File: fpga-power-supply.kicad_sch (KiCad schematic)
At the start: 30 parts, among them U14 XC7A100T-FGG484

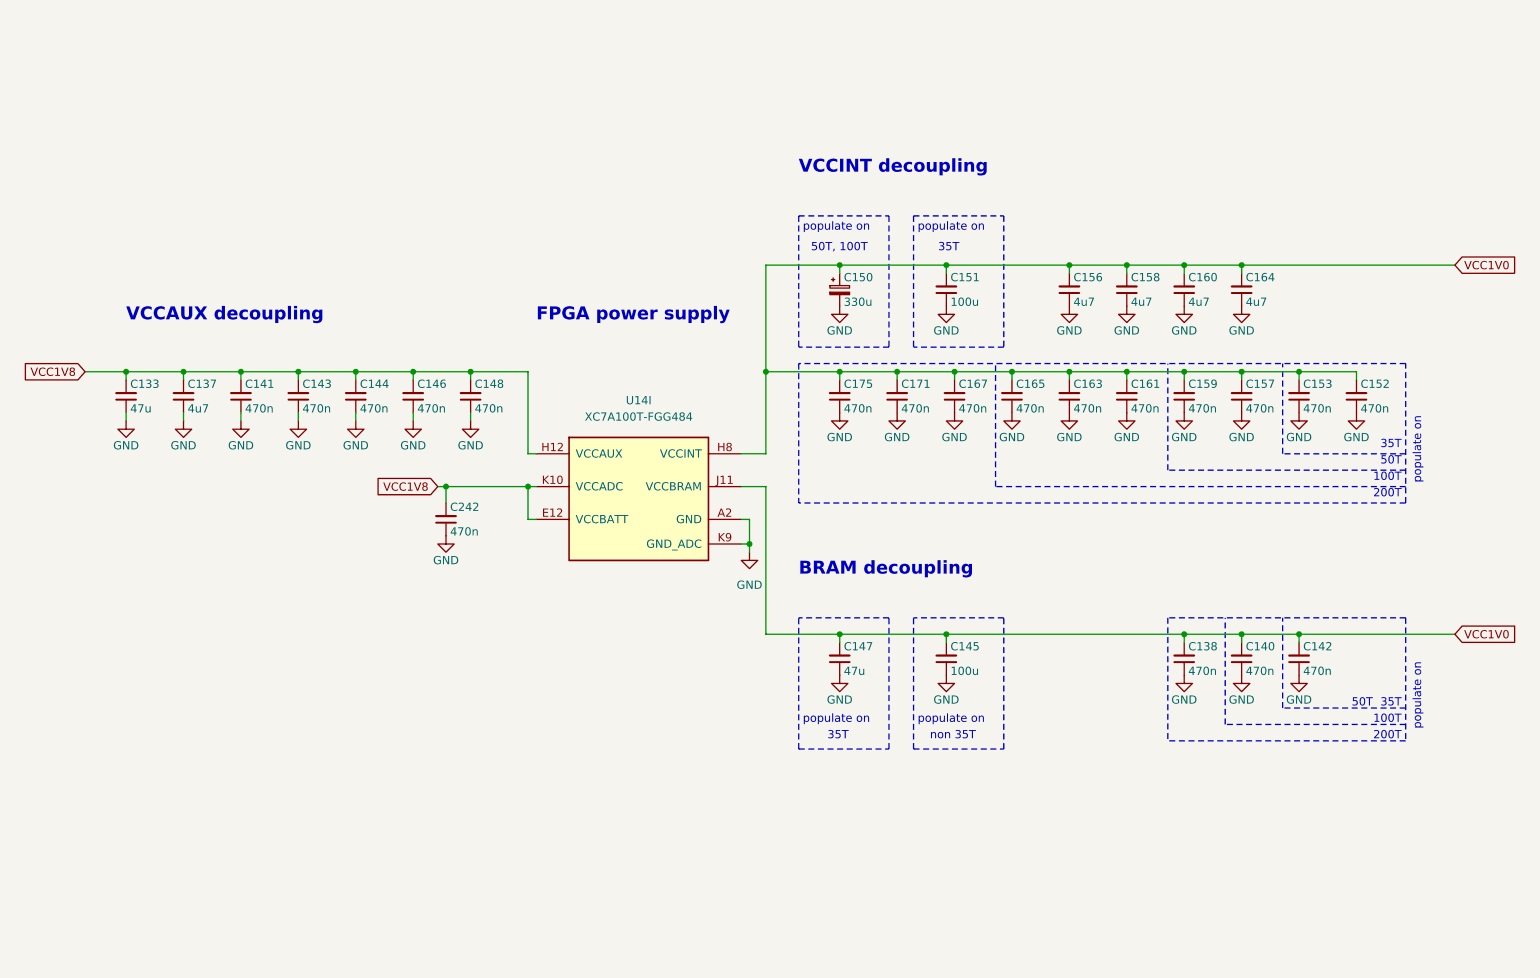
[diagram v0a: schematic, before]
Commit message: [#68236] Update symbols and footprints, clean ERC and DRC
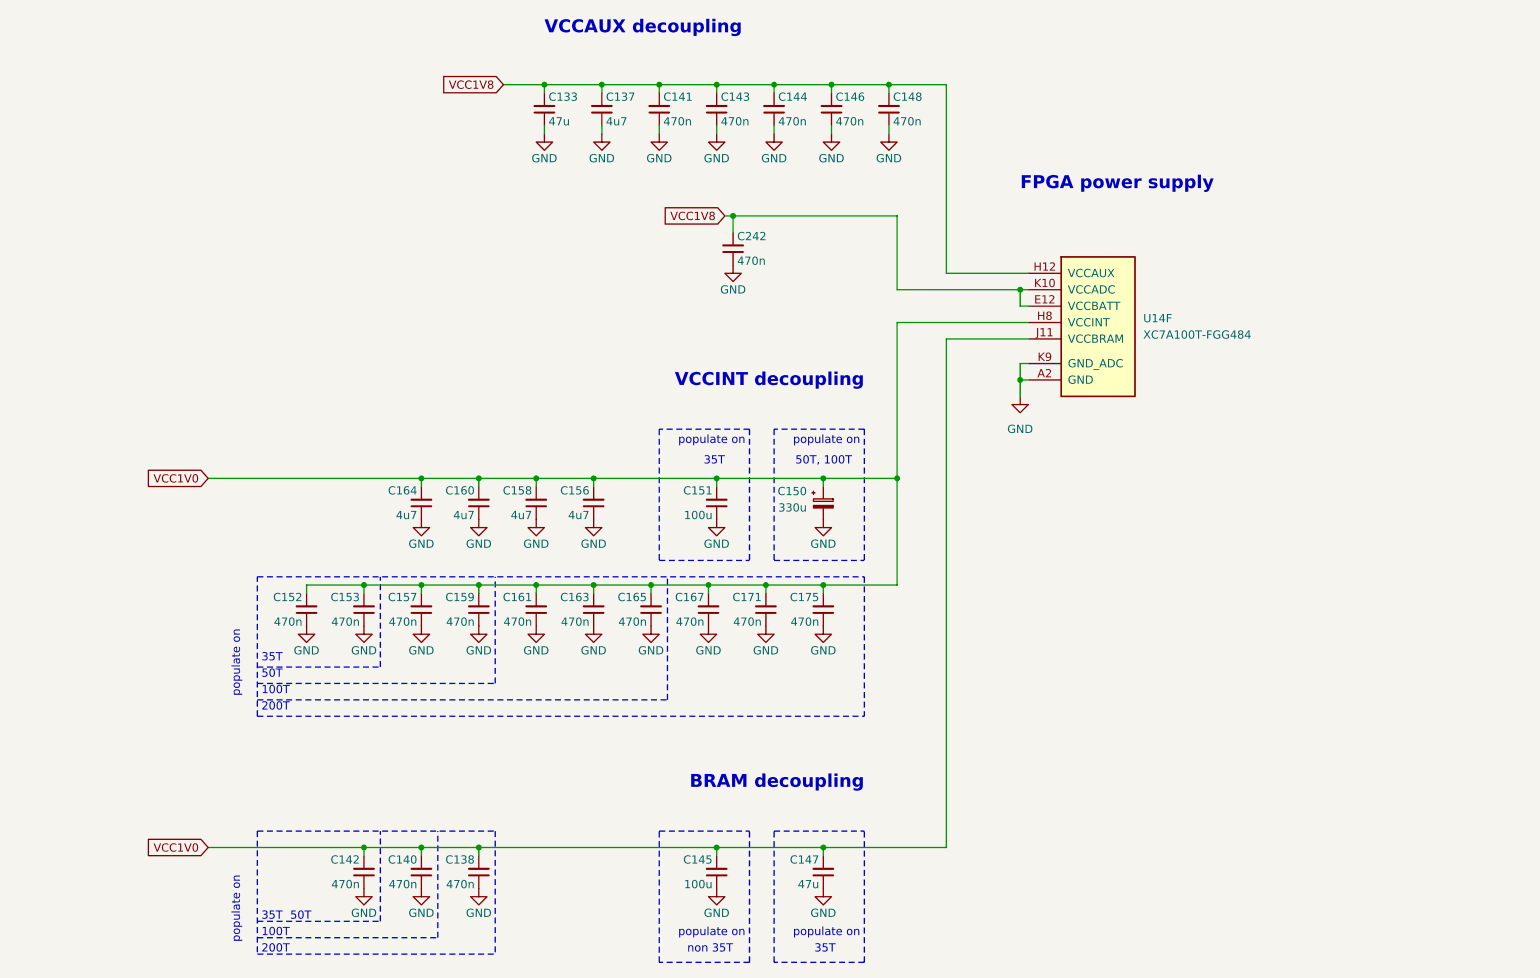
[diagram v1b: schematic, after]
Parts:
- removed U14: XC7A100T-FGG484, antmicro-footprints:BGA-484_23x23mm_Layout22x22_P1mm_FGG484, symbol antmicroFPGAChips:XC7A100T-FGG484
- added U14: XC7A100T-FGG484, antmicro-footprints:BGA-484_23x23mm_Layout22x22_P1mm_FGG484, symbol antmicroFPGAChips:XC7A100T-FGG484
- C133, C138, C142, C145, C146, C147, C151, C152, C153, C157, C159, C161, C163, C165, C171, C175, C242: Public (none) -> False
- C150: Dielectric (none) -> template_dielectric
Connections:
- net GND: now also U14.A11 (GND), U14.A12 (GND), U14.A2 (GND), U14.A22 (GND), U14.A3 (GND), U14.A5 (GND), U14.A7 (GND), U14.A9 (GND), U14.AA12 (GND), U14.AA2 (GND), U14.AA22 (GND), U14.AB19 (GND), U14.AB9 (GND), U14.B12 (GND), U14.B19 (GND), U14.B3 (GND), U14.C10 (GND), U14.C12 (GND), U14.C16 (GND), U14.C3 (GND), U14.C6 (GND), U14.D12 (GND), U14.D13 (GND), U14.D3 (GND), U14.D4 (GND), U14.D8 (GND), U14.E11 (GND), U14.E20 (GND), U14.E4 (GND), U14.E5 (GND), U14.E7 (GND), U14.E9 (GND), U14.F11 (GND), U14.F17 (GND), U14.F5 (GND), U14.G10 (GND), U14.G12 (GND), U14.G14 (GND), U14.G5 (GND), U14.G6 (GND), U14.G7 (GND), U14.G8 (GND), U14.G9 (GND), U14.H1 (GND), U14.H11 (GND), U14.H21 (GND), U14.H7 (GND), U14.H9 (GND), U14.J10 (GND), U14.J12 (GND), U14.J18 (GND), U14.J8 (GND), U14.K11 (GND), U14.K15 (GND), U14.K5 (GND), U14.K7 (GND), U14.K9 (GND_ADC), U14.L2 (GND), U14.L22 (GND), U14.L8 (GND), U14.M11 (GND), U14.M19 (GND), U14.M7 (GND), U14.N16 (GND), U14.N6 (GND), U14.N8 (GND), U14.P11 (GND), U14.P13 (GND), U14.P3 (GND), U14.P7 (GND), U14.P9 (GND), U14.R10 (GND), U14.R12 (GND), U14.R20 (GND), U14.R8 (GND), U14.T11 (GND), U14.T17 (GND), U14.T7 (GND), U14.T9 (GND), U14.U14 (GND), U14.U4 (GND), U14.V1 (GND), U14.V11 (GND), U14.V21 (GND), U14.W18 (GND), U14.W8 (GND), U14.Y15 (GND), U14.Y5 (GND)
- net VCC1V0: now also U14.H10 (VCCINT), U14.H8 (VCCINT), U14.J11 (VCCBRAM), U14.J7 (VCCINT), U14.J9 (VCCINT), U14.K8 (VCCINT), U14.L11 (VCCBRAM), U14.L7 (VCCINT), U14.M8 (VCCINT), U14.N11 (VCCBRAM), U14.N7 (VCCINT), U14.P10 (VCCINT), U14.P8 (VCCINT), U14.R7 (VCCINT), U14.R9 (VCCINT), U14.T10 (VCCINT), U14.T8 (VCCINT)
- net VCC1V8: now also U14.E12 (VCCBATT), U14.H12 (VCCAUX), U14.K10 (VCCADC), U14.K12 (VCCAUX), U14.M12 (VCCAUX), U14.P12 (VCCAUX), U14.R11 (VCCAUX)
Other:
- moved on the sheet: C133, C137, C141, C143, C144, C146, C148, C242

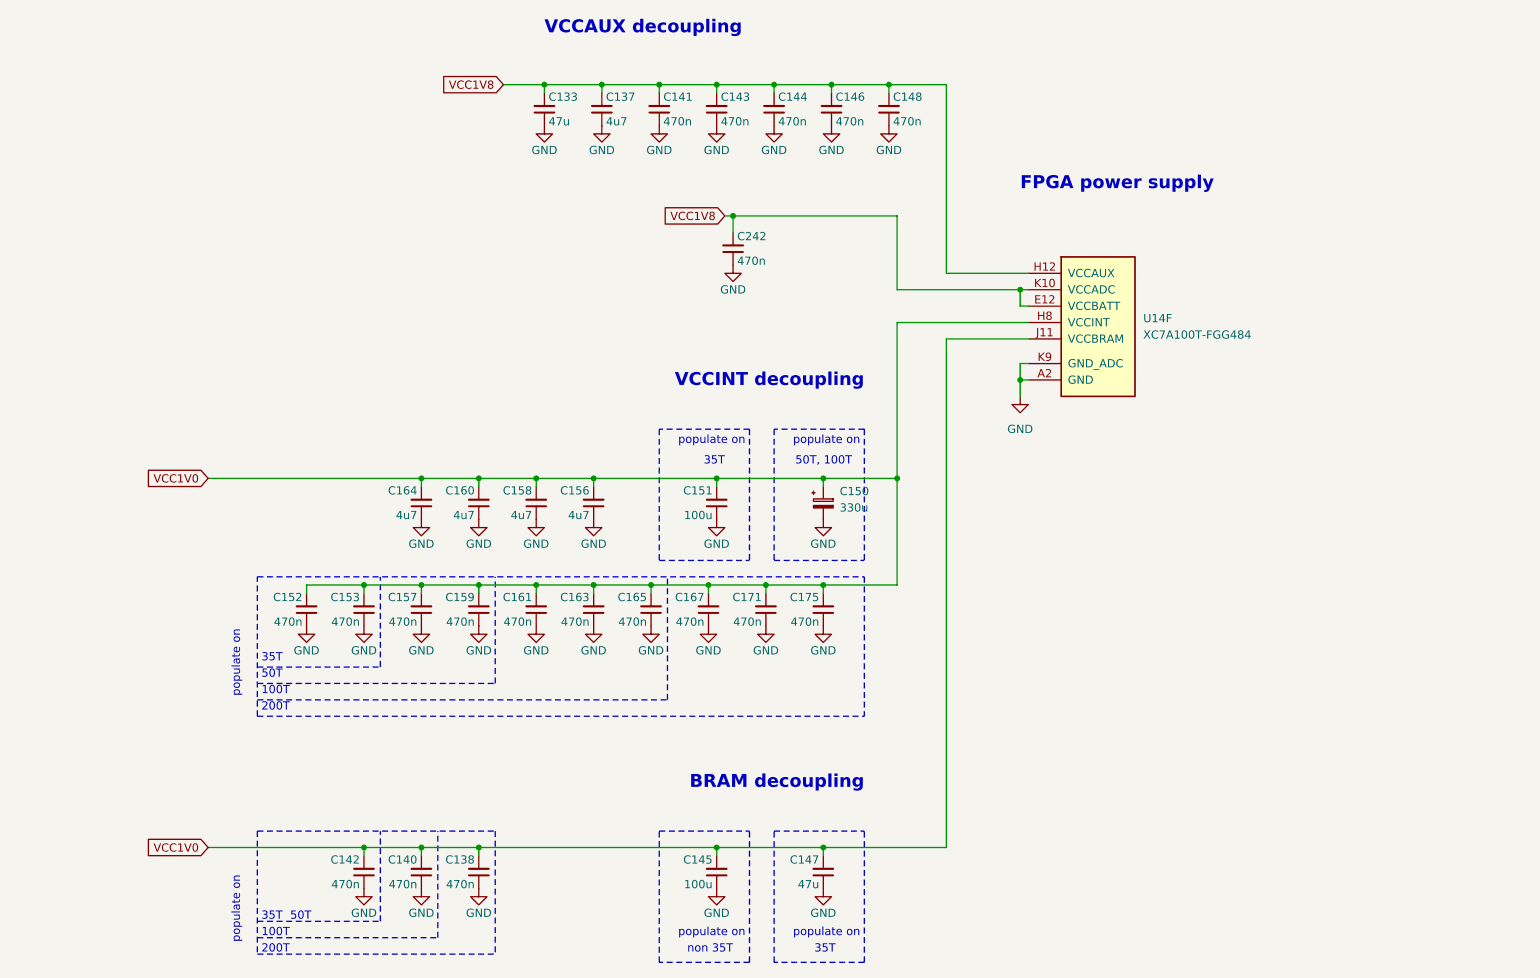
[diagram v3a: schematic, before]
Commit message: a lot of routing and almost all caps of the fpga are placed down
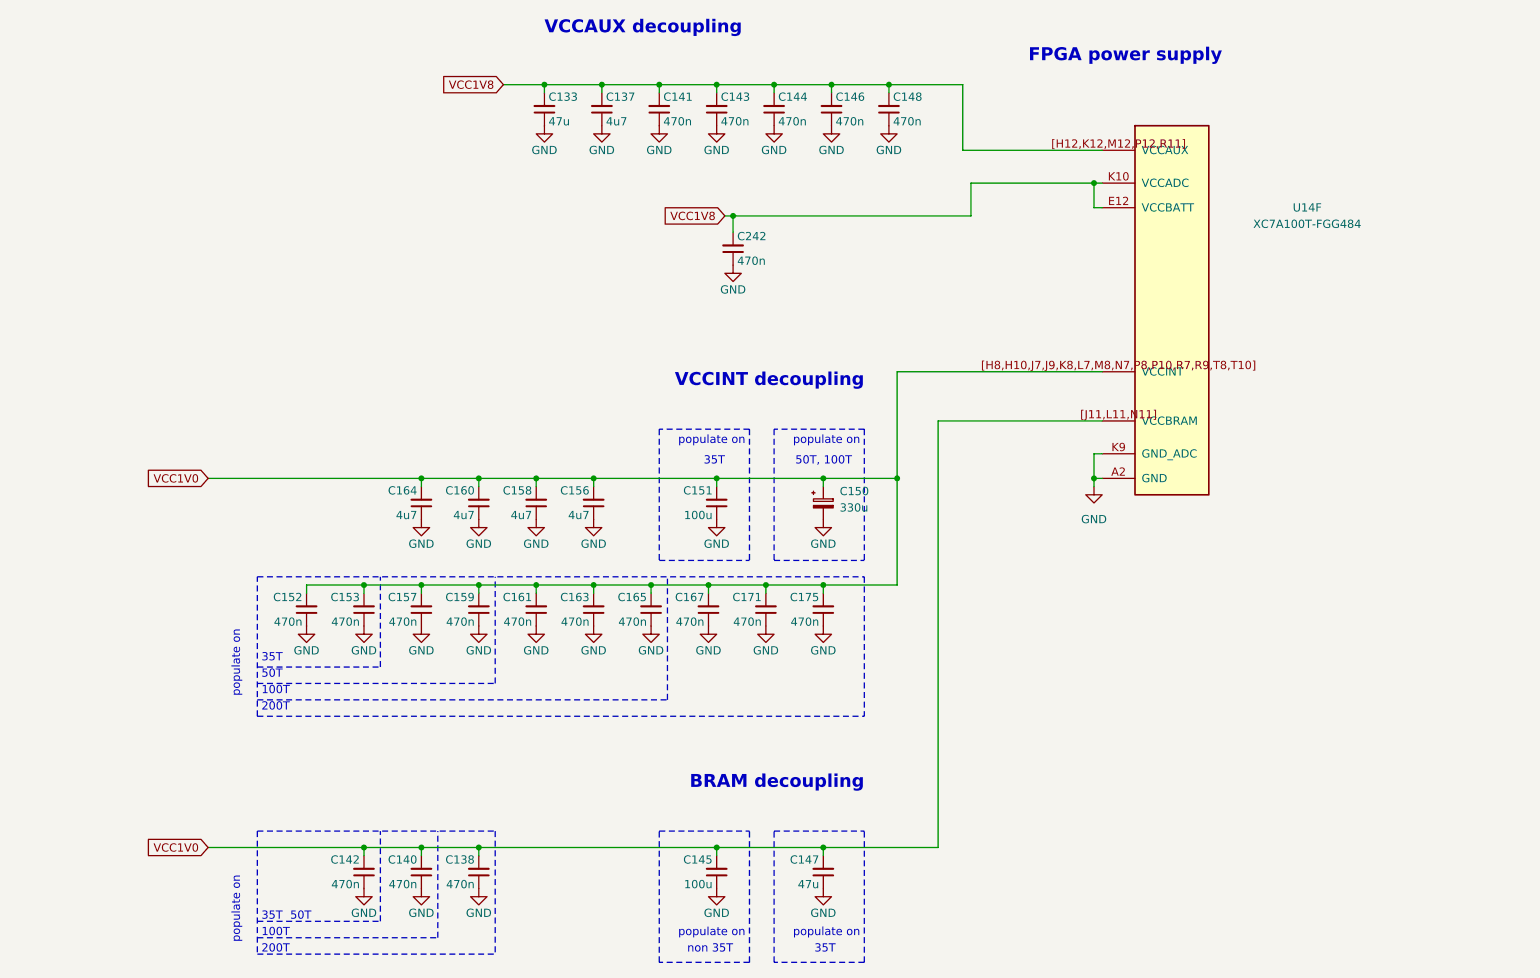
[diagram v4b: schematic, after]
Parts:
- C137, C156, C158, C160, C164: footprint antmicro-footprints:C_0603_1608Metric -> Capacitor_SMD:C_0603_1608Metric; MPN C1608X5R1V475M080AC -> C0603C475K9PAC; Manufacturer TDK -> KEMET
- C140, C141, C143, C144, C148, C167: footprint antmicro-footprints:C_0402_1005Metric -> Capacitor_SMD:C_0402_1005Metric
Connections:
- net VCC1V0: now also U14.[H8,H10,J7,J9,K8,L7,M8,N7,P8,P10,R7,R9,T8,T10] (VCCINT), U14.[J11,L11,N11] (VCCBRAM); no longer U14.H10 (VCCINT), U14.H8 (VCCINT), U14.J11 (VCCBRAM), U14.J7 (VCCINT), U14.J9 (VCCINT), U14.K8 (VCCINT), U14.L11 (VCCBRAM), U14.L7 (VCCINT), U14.M8 (VCCINT), U14.N11 (VCCBRAM), U14.N7 (VCCINT), U14.P10 (VCCINT), U14.P8 (VCCINT), U14.R7 (VCCINT), U14.R9 (VCCINT), U14.T10 (VCCINT), U14.T8 (VCCINT)
- net VCC1V8: now also U14.[H12,K12,M12,P12,R11] (VCCAUX); no longer U14.H12 (VCCAUX), U14.K12 (VCCAUX), U14.M12 (VCCAUX), U14.P12 (VCCAUX), U14.R11 (VCCAUX)

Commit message: a lot of poin swaps
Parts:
- C138, C142, C146, C152, C153, C157, C159, C161, C163, C165, C171, C175, C242: value C_470n_0201 -> C_470n_0402; footprint antmicro-footprints:C_0201 -> Capacitor_SMD:C_0402_1005Metric; MPN C0603X5R1A474M030BC -> GXT155C80J474KE01D; Manufacturer TDK -> Murata Electronics
- C140, C141, C143, C144, C148, C167: MPN C1005X5R1E474M050BB -> GXT155C80J474KE01D; Manufacturer TDK -> Murata Electronics

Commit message: version 1.0 complete
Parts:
- C133, C147: MPN C1210C476K8RACTU -> C1210C476K8RAC7210
- U14: MPN XC7A100T-FGG484 -> XC7A100T-2FGG484C

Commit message: "In the process of upgrading the ddr memory"
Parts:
- C133, C145, C147, C151: footprint antmicro-footprints:C_1210_3225Metric -> Capacitor_SMD:C_1210_3225Metric
